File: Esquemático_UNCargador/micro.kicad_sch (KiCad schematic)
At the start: 34 parts, among them J4 Conn_01x02, J6 Conn_01x08_Pin, SW10 SW_Push, SW6 SW_Push, SW7 SW_Push, SW8 SW_Push, SW9 SW_Push, U2 W25Q128JVS, U3 RP2040, Y1 ABLS-12.000MHZ-B4-T

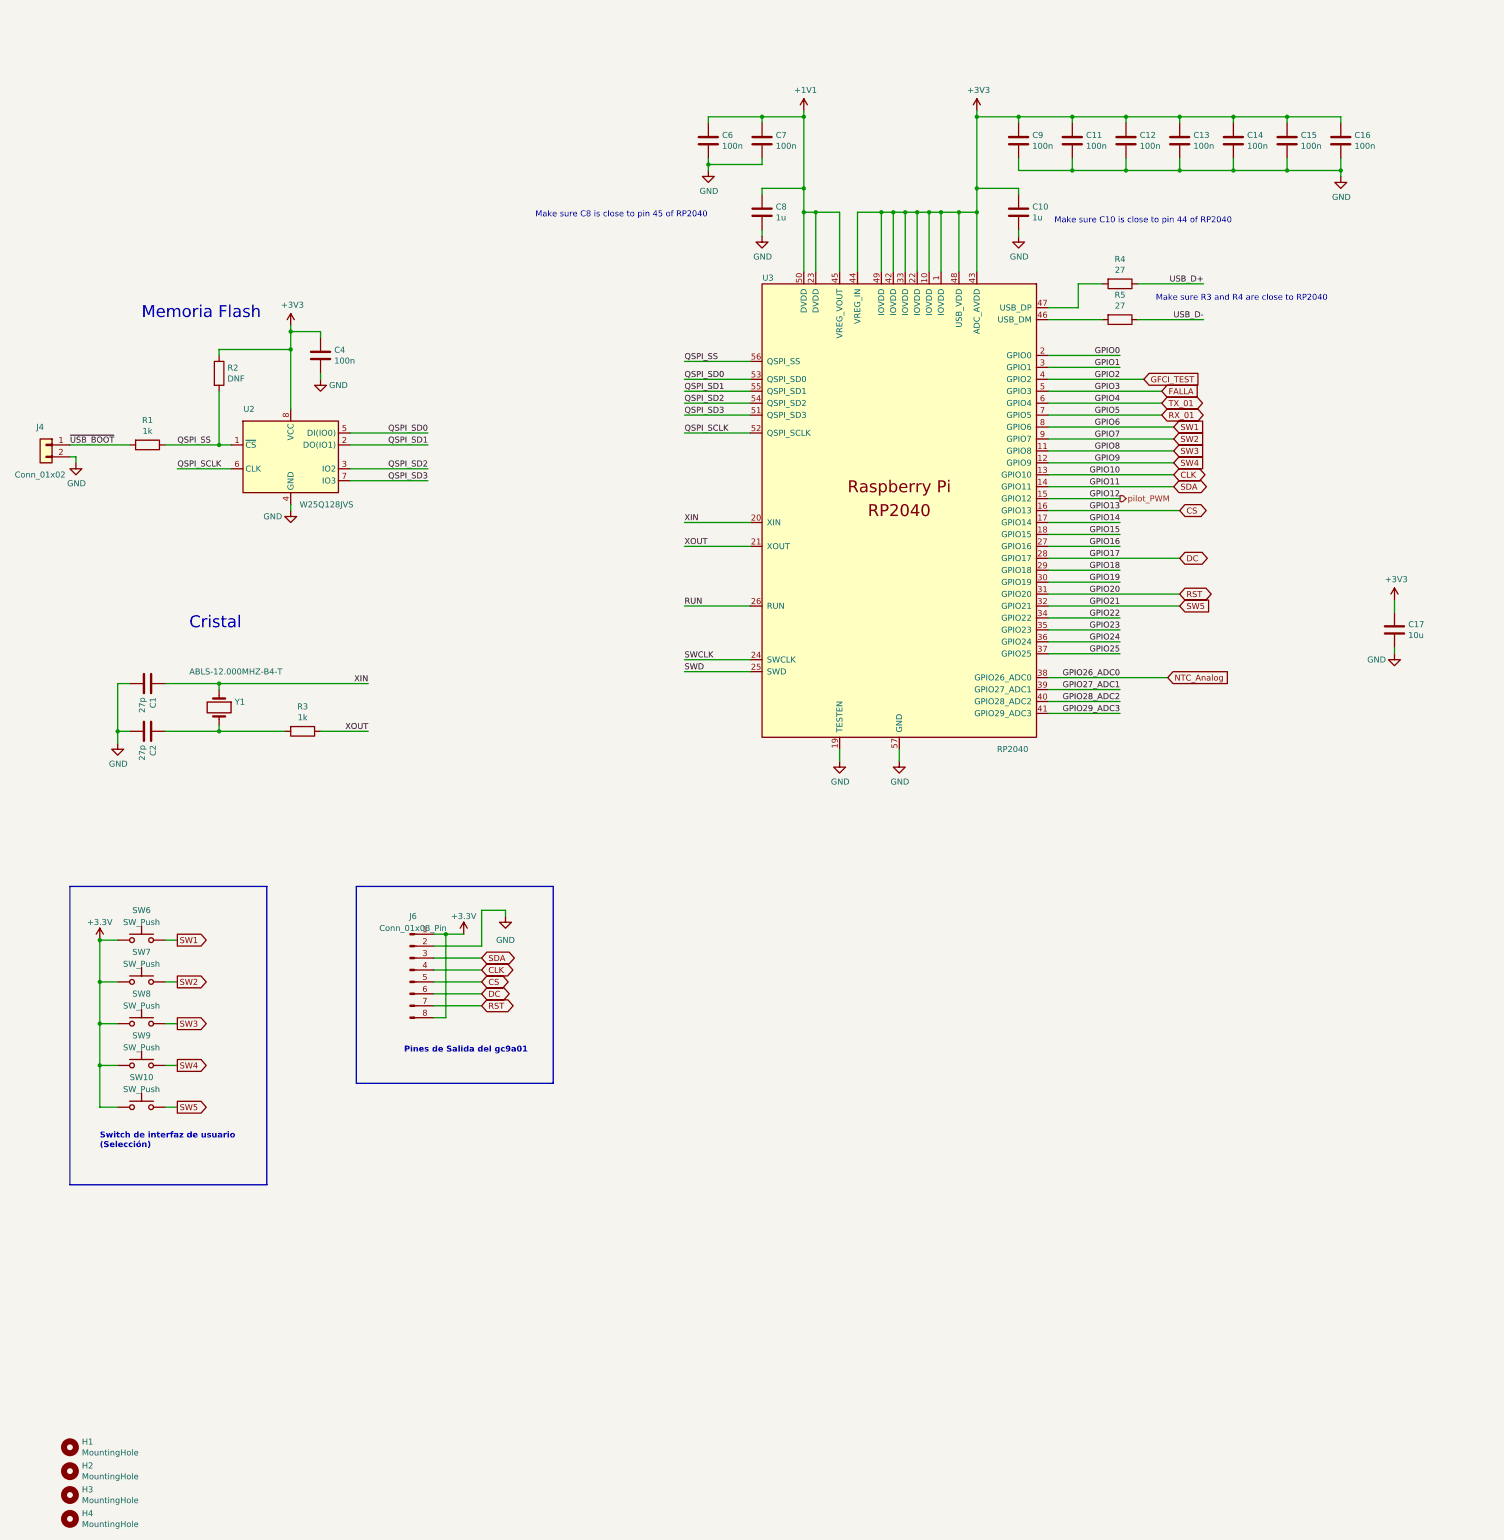
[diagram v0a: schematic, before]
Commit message: Se modifica esquema del micro y se agrega página de sensores
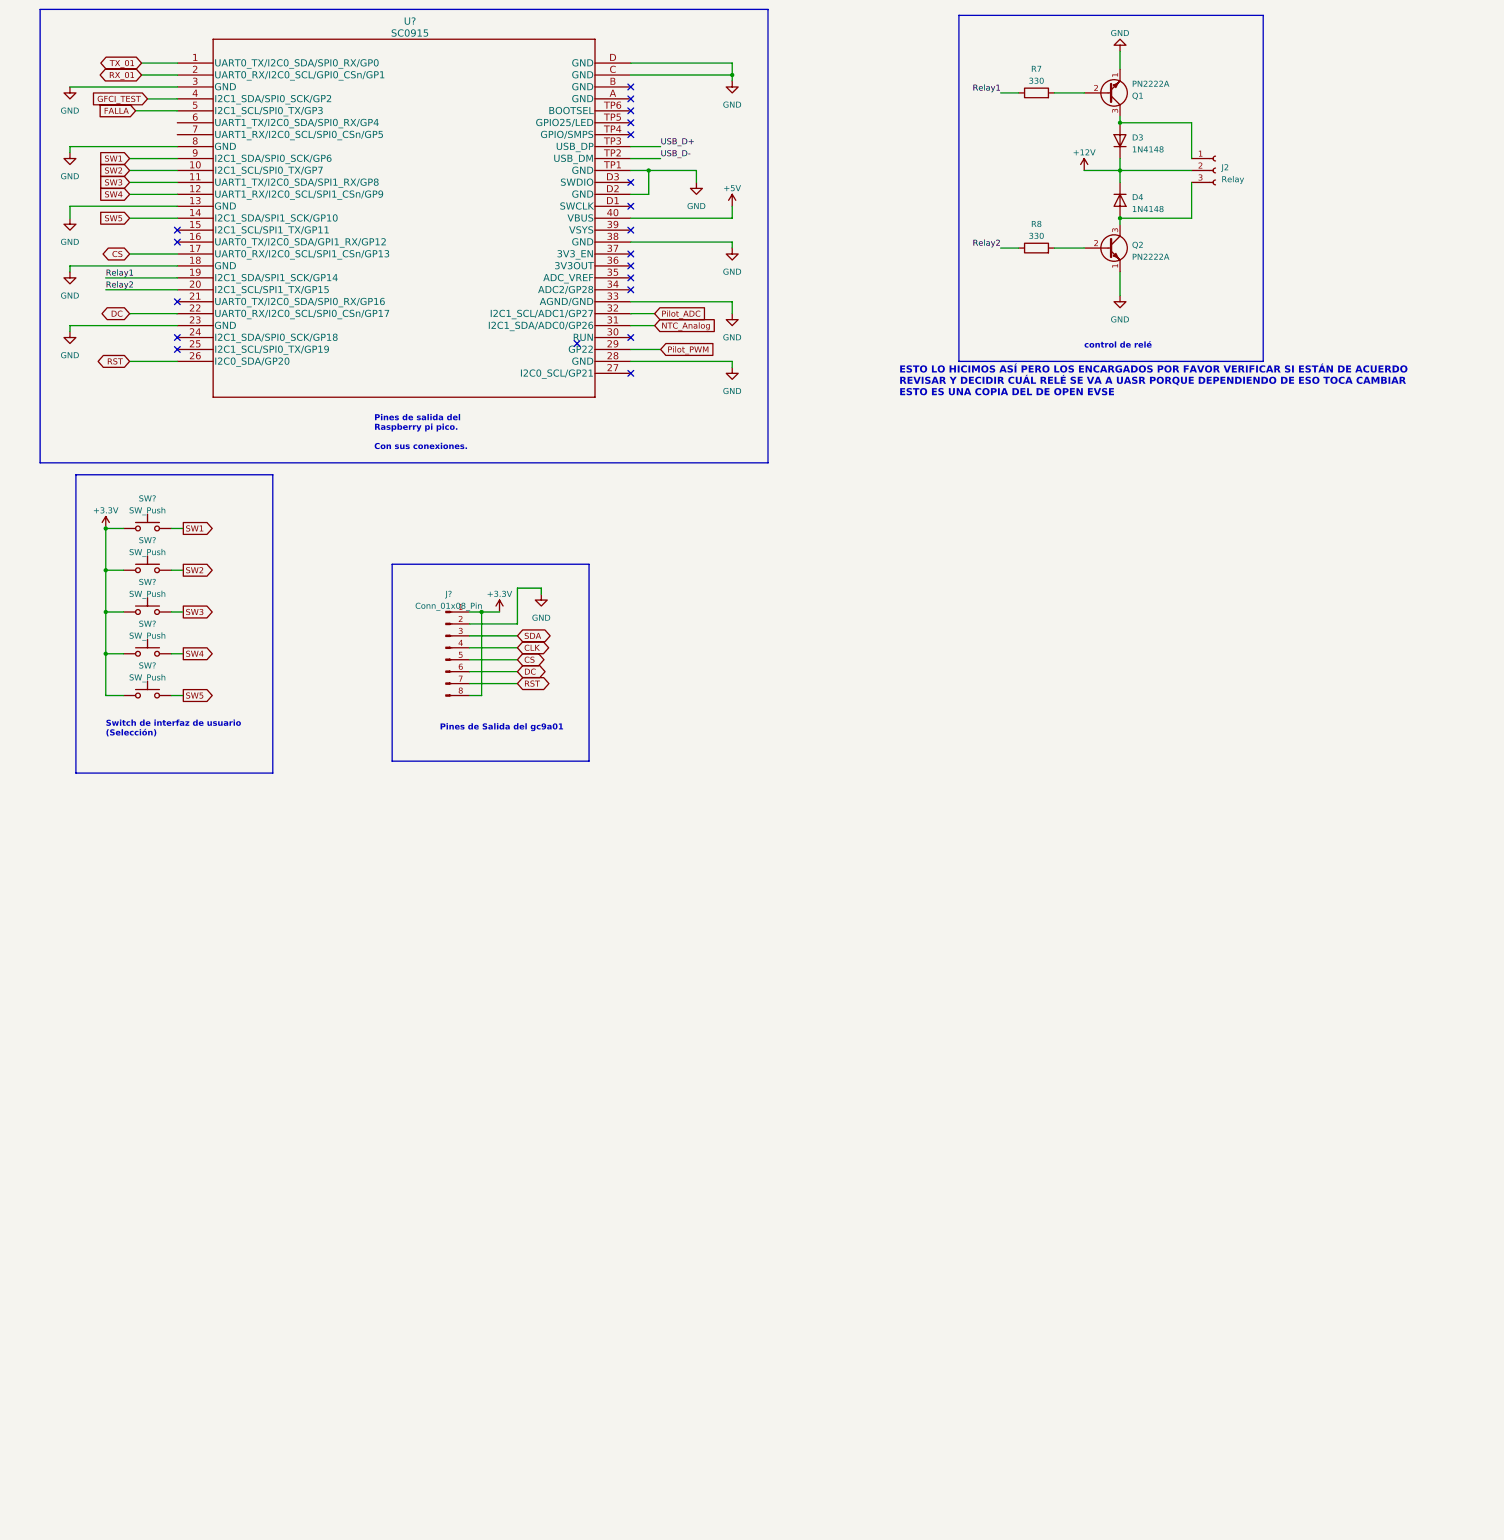
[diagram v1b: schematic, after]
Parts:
- removed C1, C2: 27p, Capacitor_SMD:C_0402_1005Metric, symbol Device:C
- removed C10, C8: 1u, Capacitor_SMD:C_0402_1005Metric, symbol Device:C
- removed C11, C12, C13, C14, C15, C16, C4, C6, C7, C9: 100n, Capacitor_SMD:C_0402_1005Metric, symbol Device:C
- removed C17: 10u, Capacitor_SMD:C_0805_2012Metric, symbol Device:C
- removed H1, H2, H3, H4: MountingHole, MountingHole:MountingHole_2.7mm_M2.5, symbol Mechanical:MountingHole
- removed J4: Conn_01x02, Connector_PinHeader_2.54mm:PinHeader_1x02_P2.54mm_Vertical, symbol Connector_Generic:Conn_01x02
- removed J6: Conn_01x08_Pin, symbol Connector:Conn_01x08_Pin
- removed R1, R3: 1k, Capacitor_SMD:C_0402_1005Metric, symbol Device:R
- removed R2: DNF, Capacitor_SMD:C_0402_1005Metric, symbol Device:R
- removed R4, R5: 27, Capacitor_SMD:C_0402_1005Metric, symbol Device:R
- removed SW10, SW6, SW7, SW8, SW9: SW_Push, symbol Switch:SW_Push
- removed U2: W25Q128JVS, Package_SO:SOIC-8_5.23x5.23mm_P1.27mm, symbol RP2040_minimal-rescue:W25Q128JVS-Memory_Flash
- removed U3: RP2040, RP2040_minimal:RP2040-QFN-56, symbol MCU_RaspberryPi_RP2040:RP2040
- removed Y1: ABLS-12.000MHZ-B4-T, RP2040_minimal:Crystal_SMD_HC49-US, symbol Device:Crystal
- added D3, D4: 1N4148, Diode_THT:D_DO-35_SOD27_P7.62mm_Horizontal, symbol Diode:1N4148
- added J2: Relay, symbol Connector:Conn_01x03_Socket
- added J?: Conn_01x08_Pin, symbol Connector:Conn_01x08_Pin
- added Q1, Q2: PN2222A, Package_TO_SOT_THT:TO-92_Inline, symbol Transistor_BJT:PN2222A
- added R7, R8: 330, symbol Device:R
- added SW? (x5): SW_Push, symbol Switch:SW_Push
- added U?: SC0915, RP2040:RP2040_SC0915, symbol RP2040:SC0915
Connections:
- net +3.3V: now also J?.1 (Pin_1), J?.8 (Pin_8), SW?.1, SW?.1, SW?.1, SW?.1, SW?.1
- net CLK: now also J?.4 (Pin_4)
- net CS: now also J?.5 (Pin_5), U?.17 (UART0_RX/I2C0_SCL/SPI1_CSn/GP13)
- net DC: now also J?.6 (Pin_6), U?.22 (UART0_RX/I2C0_SCL/SPI0_CSn/GP17)
- net FALLA: now also U?.5 (I2C1_SCL/SPI0_TX/GP3)
- net GFCI_TEST: now also U?.4 (I2C1_SDA/SPI0_SCK/GP2)
- net GND: now also J?.2 (Pin_2), Q1.1 (E), Q2.1 (E), U?.13 (GND), U?.18 (GND), U?.23 (GND), U?.28 (GND), U?.3 (GND), U?.33 (AGND/GND), U?.38 (GND), U?.8 (GND), U?.C (GND), U?.D (GND), U?.D2 (GND), U?.TP1 (GND)
- net NTC_Analog: now also U?.31 (I2C1_SDA/ADC0/GP26)
- net RST: now also J?.7 (Pin_7), U?.26 (I2C0_SDA/GP20)
- net RX_01: now also U?.2 (UART0_RX/I2C0_SCL/GPI0_CSn/GP1)
- net SDA: now also J?.3 (Pin_3)
- net SW1: now also SW?.2, U?.9 (I2C1_SDA/SPI0_SCK/GP6)
- net SW2: now also SW?.2, U?.10 (I2C1_SCL/SPI0_TX/GP7)
- net SW3: now also SW?.2, U?.11 (UART1_TX/I2C0_SDA/SPI1_RX/GP8)
- net SW4: now also SW?.2, U?.12 (UART1_RX/I2C0_SCL/SPI1_CSn/GP9)
- net SW5: now also SW?.2, U?.14 (I2C1_SDA/SPI1_SCK/GP10)
- net TX_01: now also U?.1 (UART0_TX/I2C0_SDA/SPI0_RX/GP0)
- net USB_D+: now also U?.TP3 (USB_DP)
- net USB_D-: now also U?.TP2 (USB_DM)
- new net: Q2.2 (B), R8.2
- new net: Q1.2 (B), R7.2
- new net: D4.2 (A), J2.3 (Pin_3), Q2.3 (C)
- new net: D3.2 (A), J2.1 (Pin_1), Q1.3 (C)
- new net +12V: D3.1 (K), D4.1 (K), J2.2 (Pin_2)
- new net +5V: U?.40 (VBUS)
- new net Pilot_ADC: U?.32 (I2C1_SCL/ADC1/GP27)
- new net Pilot_PWM: U?.29 (GP22)
- new net Relay1: R7.1, U?.19 (I2C1_SDA/SPI1_SCK/GP14)
- new net Relay2: R8.1, U?.20 (I2C1_SCL/SPI1_TX/GP15)
- no-connect marks 0 -> 20
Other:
- note added: "ESTO LO HICIMOS ASÍ PERO LOS ENCARGADOS POR FAVOR VERIFICAR SI ESTÁN DE ACUERDO REVISAR Y DECIDIR CUÁL RELÉ SE VA A UASR PORQUE DEPENDIENDO DE ESO TOCA CAMBIAR ESTO ES UNA COPIA DEL DE OPEN EVSE"
- note added: "Pines de salida del Raspberry pi pico. Con sus conexiones."
- note added: "control de relé"
- note removed: "Cristal"
- note removed: "Make sure C10 is close to pin 44 of RP2040"
- note removed: "Make sure C8 is close to pin 45 of RP2040"
- note removed: "Make sure R3 and R4 are close to RP2040"
- note removed: "Memoria Flash"
- company: (none) -> UNIVERSIDAD NACIONAL DE COLOMBIA
- title: (none) -> Esquema pines micro

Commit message: Pinout sensores
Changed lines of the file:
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@@
-    )
-  )
-  (global_label "NTC_Analog" (shape input) (at 154.94 91.44 0) (fields_autoplaced)
-    (effects (font (size 1.27 1.27)) (justify left))
-    (property "Intersheetrefs" "${INTERSHEET_REFS}" (at 168.7313 91.44 0)
-      (effects (font (size 1.27 1.27)) (justify left) hide)
     )
   )
@@
     )
   )
-  (global_label "RX_01" (shape bidirectional) (at 45.72 38.1 180) (fields_autoplaced)
-    (effects (font (size 1.27 1.27)) (justify right))
-    (property "Intersheetrefs" "${INTERSHEET_REFS}" (at 35.8368 38.1 0)
-      (effects (font (size 1.27 1.27)) (justify right) hide)
-    )
-  )
-  (global_label "FALLA" (shape input) (at 44.45 45.72 180) (fields_autoplaced)
-    (effects (font (size 1.27 1.27)) (justify right))
-    (property "Intersheetrefs" "${INTERSHEET_REFS}" (at 36.2222 45.72 0)
-      (effects (font (size 1.27 1.27)) (justify right) hide)
-    )
-  )
   (global_label "SW1" (shape input) (at 43.18 55.88 180) (fields_autoplaced)
     (effects (font (size 1.27 1.27)) (justify right))
@@
     (property "Intersheetrefs" "${INTERSHEET_REFS}" (at 61.3862 170.18 0)
       (effects (font (size 1.27 1.27)) (justify left) hide)
-    )
-  )
-  (global_label "TX_01" (shape bidirectional) (at 45.72 35.56 180) (fields_autoplaced)
-    (effects (font (size 1.27 1.27)) (justify right))
-    (property "Intersheetrefs" "${INTERSHEET_REFS}" (at 36.1392 35.56 0)
-      (effects (font (size 1.27 1.27)) (justify right) hide)
     )
   )
@@
     )
   )
-  (global_label "GFCI_TEST" (shape input) (at 46.99 43.18 180) (fields_autoplaced)
-    (effects (font (size 1.27 1.27)) (justify right))
-    (property "Intersheetrefs" "${INTERSHEET_REFS}" (at 34.5895 43.18 0)
-      (effects (font (size 1.27 1.27)) (justify right) hide)
-    )
-  )
   (global_label "CLK" (shape bidirectional) (at 125.73 160.02 0) (fields_autoplaced)
     (effects (font (size 1.27 1.27)) (justify left))
@@
     )
   )
+  (hierarchical_label "FALLA" (shape input) (at 44.45 45.72 180) (fields_autoplaced)
+    (effects (font (size 1.27 1.27)) (justify right))
+  )
+  (hierarchical_label "NTC_Analog" (shape input) (at 154.94 91.44 0) (fields_autoplaced)
+    (effects (font (size 1.27 1.27)) (justify left))
+  )
+  (hierarchical_label "RX_01" (shape input) (at 45.72 38.1 180) (fields_autoplaced)
+    (effects (font (size 1.27 1.27)) (justify right))
+  )
+  (hierarchical_label "TX_01" (shape input) (at 45.72 35.56 180) (fields_autoplaced)
+    (effects (font (size 1.27 1.27)) (justify right))
+  )
+  (hierarchical_label "GFCI_TEST" (shape input) (at 46.99 43.18 180) (fields_autoplaced)
+    (effects (font (size 1.27 1.27)) (justify right))
+  )
   (symbol (lib_id "Switch:SW_Push") (at 46.99 143.51 0) (unit 1)

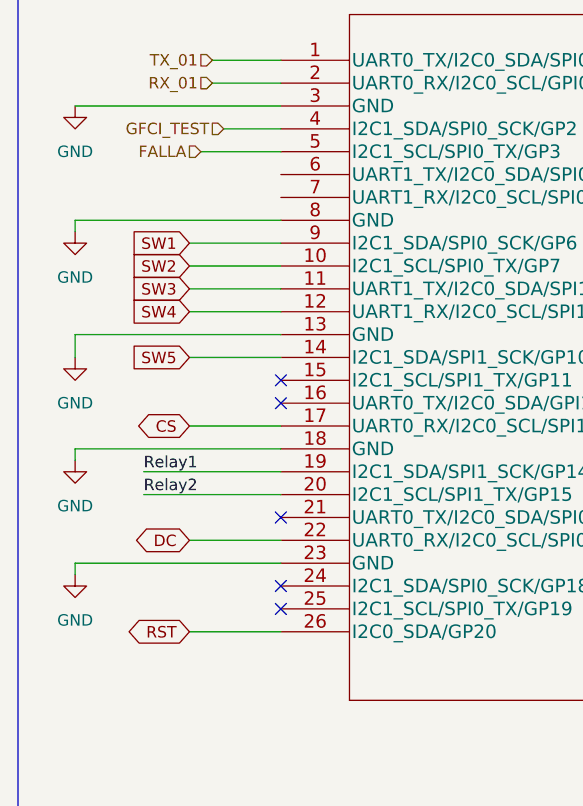
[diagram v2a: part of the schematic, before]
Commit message: Cambio de pantalla
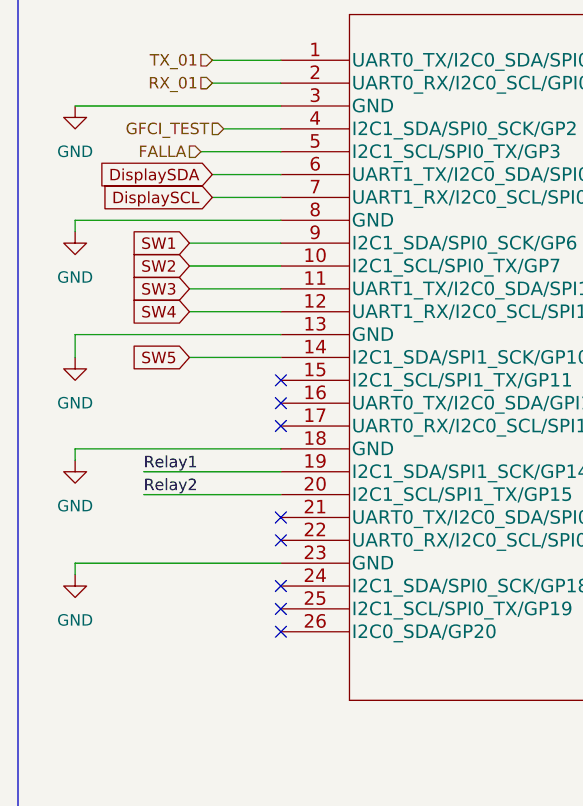
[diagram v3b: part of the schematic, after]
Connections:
- net CS: no longer U?.17 (UART0_RX/I2C0_SCL/SPI1_CSn/GP13)
- net DC: no longer U?.22 (UART0_RX/I2C0_SCL/SPI0_CSn/GP17)
- net RST: no longer U?.26 (I2C0_SDA/GP20)
- net DisplaySDA: now reaches U?.6 (UART1_TX/I2C0_SDA/SPI0_RX/GP4)
- net DisplaySCL: now reaches U?.7 (UART1_RX/I2C0_SCL/SPI0_CSn/GP5)
- no-connect marks 20 -> 23
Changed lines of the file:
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@@
   (no_connect (at 138.43 95.25))
   (no_connect (at 149.86 48.26))
+  (no_connect (at 53.34 76.2))
+  (no_connect (at 53.34 88.9))
   (no_connect (at 149.86 78.74))
   (no_connect (at 149.86 40.64))
@@
   (no_connect (at 149.86 76.2))
   (no_connect (at 149.86 81.28))
+  (no_connect (at 53.34 99.06))
   (no_connect (at 149.86 60.96))
   (no_connect (at 53.34 96.52))
@@
     (stroke (width 0) (type default))
   )
-  (wire (pts (xy 43.18 88.9) (xy 53.34 88.9))
-    (stroke (width 0) (type default))
-  )
   (wire (pts (xy 45.72 35.56) (xy 53.34 35.56))
     (stroke (width 0) (type default))
@@
     (stroke (width 0) (type default))
   )
+  (wire (pts (xy 45.72 50.8) (xy 53.34 50.8))
+    (stroke (width 0) (type default))
+  )
   (wire (pts (xy 246.38 58.42) (xy 254 58.42))
     (stroke (width 0) (type default))
@@
     (stroke (width 0) (type default))
   )
+  (wire (pts (xy 45.72 48.26) (xy 53.34 48.26))
+    (stroke (width 0) (type default))
+  )
   (wire (pts (xy 38.1 81.28) (xy 53.34 81.28))
     (stroke (width 0) (type default))
   )
-  (wire (pts (xy 43.18 76.2) (xy 53.34 76.2))
-    (stroke (width 0) (type default))
-  )
   (wire (pts (xy 41.91 152.4) (xy 38.1 152.4))
     (stroke (width 0) (type default))
@@
   )
   (wire (pts (xy 149.86 88.9) (xy 154.94 88.9))
-    (stroke (width 0) (type default))
-  )
-  (wire (pts (xy 43.18 99.06) (xy 53.34 99.06))
     (stroke (width 0) (type default))
   )
@@
     )
   )
-  (global_label "RST" (shape bidirectional) (at 43.18 99.06 180) (fields_autoplaced)
-    (effects (font (size 1.27 1.27)) (justify right))
-    (property "Intersheetrefs" "${INTERSHEET_REFS}" (at 35.7158 99.06 0)
-      (effects (font (size 1.27 1.27)) (justify right) hide)
-    )
-  )
   (global_label "SW3" (shape input) (at 43.18 60.96 180) (fields_autoplaced)
     (effects (font (size 1.27 1.27)) (justify right))
@@
     )
   )
+  (global_label "DisplaySCL" (shape input) (at 45.72 50.8 180) (fields_autoplaced)
+    (effects (font (size 1.27 1.27)) (justify right))
+    (property "Intersheetrefs" "${INTERSHEET_REFS}" (at 32.4729 50.8 0)
+      (effects (font (size 1.27 1.27)) (justify right) hide)
+    )
+  )
   (global_label "SW3" (shape output) (at 54.61 152.4 0) (fields_autoplaced)
     (effects (font (size 1.27 1.27)) (justify left))
@@
     )
   )
+  (global_label "DisplaySDA" (shape input) (at 45.72 48.26 180) (fields_autoplaced)
+    (effects (font (size 1.27 1.27)) (justify right))
+    (property "Intersheetrefs" "${INTERSHEET_REFS}" (at 32.4124 48.26 0)
+      (effects (font (size 1.27 1.27)) (justify right) hide)
+    )
+  )
   (global_label "SW2" (shape output) (at 54.61 143.51 0) (fields_autoplaced)
     (effects (font (size 1.27 1.27)) (justify left))
@@
     )
   )
-  (global_label "CS" (shape bidirectional) (at 43.18 76.2 180) (fields_autoplaced)
-    (effects (font (size 1.27 1.27)) (justify right))
-    (property "Intersheetrefs" "${INTERSHEET_REFS}" (at 36.6834 76.2 0)
-      (effects (font (size 1.27 1.27)) (justify right) hide)
-    )
-  )
   (global_label "Pilot_PWM" (shape input) (at 156.21 96.52 0) (fields_autoplaced)
     (effects (font (size 1.27 1.27)) (justify left))
@@
     )
   )
-  (global_label "DC" (shape bidirectional) (at 43.18 88.9 180) (fields_autoplaced)
-    (effects (font (size 1.27 1.27)) (justify right))
-    (property "Intersheetrefs" "${INTERSHEET_REFS}" (at 36.6229 88.9 0)
-      (effects (font (size 1.27 1.27)) (justify right) hide)
-    )
-  )
